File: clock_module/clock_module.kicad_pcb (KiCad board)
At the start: 2 copper layers, 100 x 100 mm, 38 parts, among them J1 USB_C_Receptacle_PowerOnly_6P, J2 Conn_01x02_Socket, SW1 SW_Push, SW2 SW_SPDT, SW3 SW_SPDT, SW4 SW_SPST, U1 74HC14

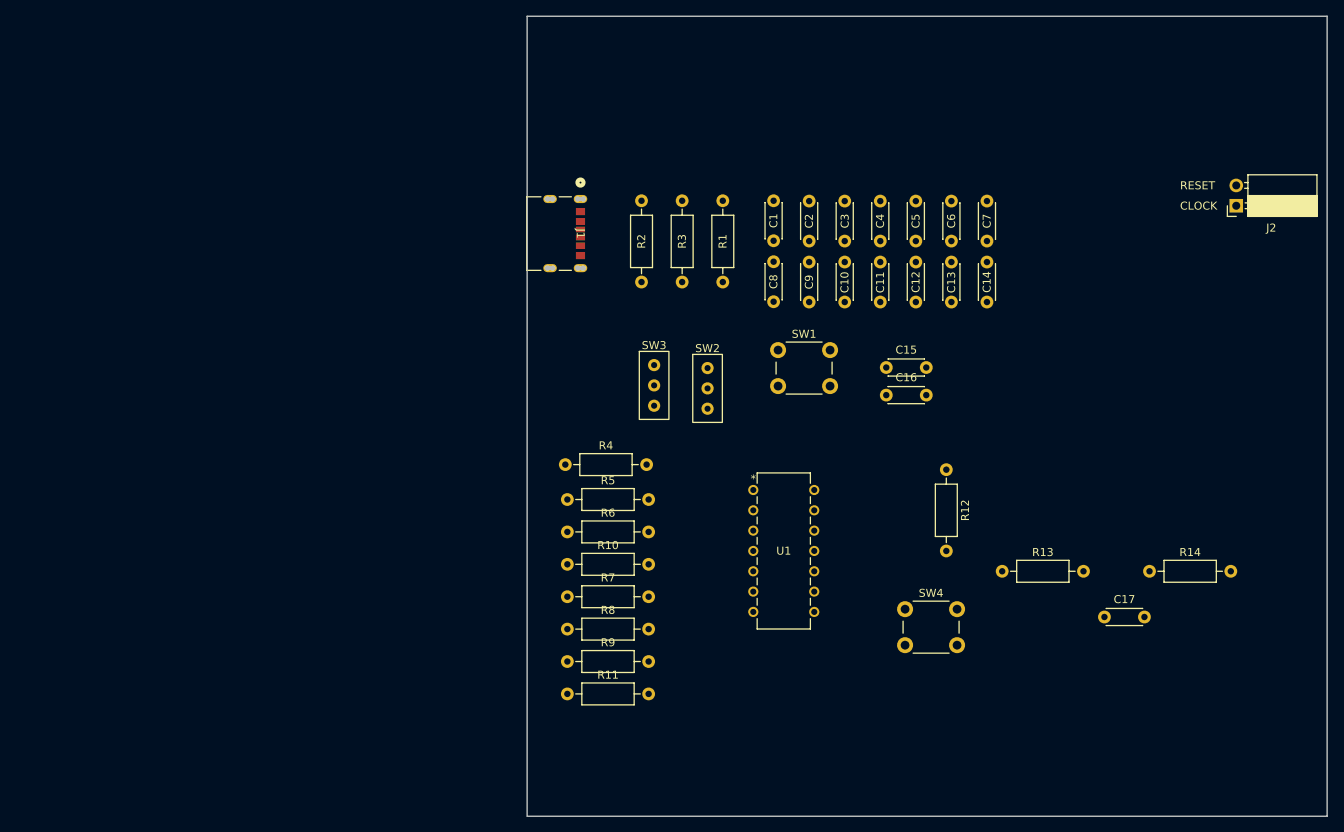
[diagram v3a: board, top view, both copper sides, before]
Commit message: クロック、リセット回路の基盤設計
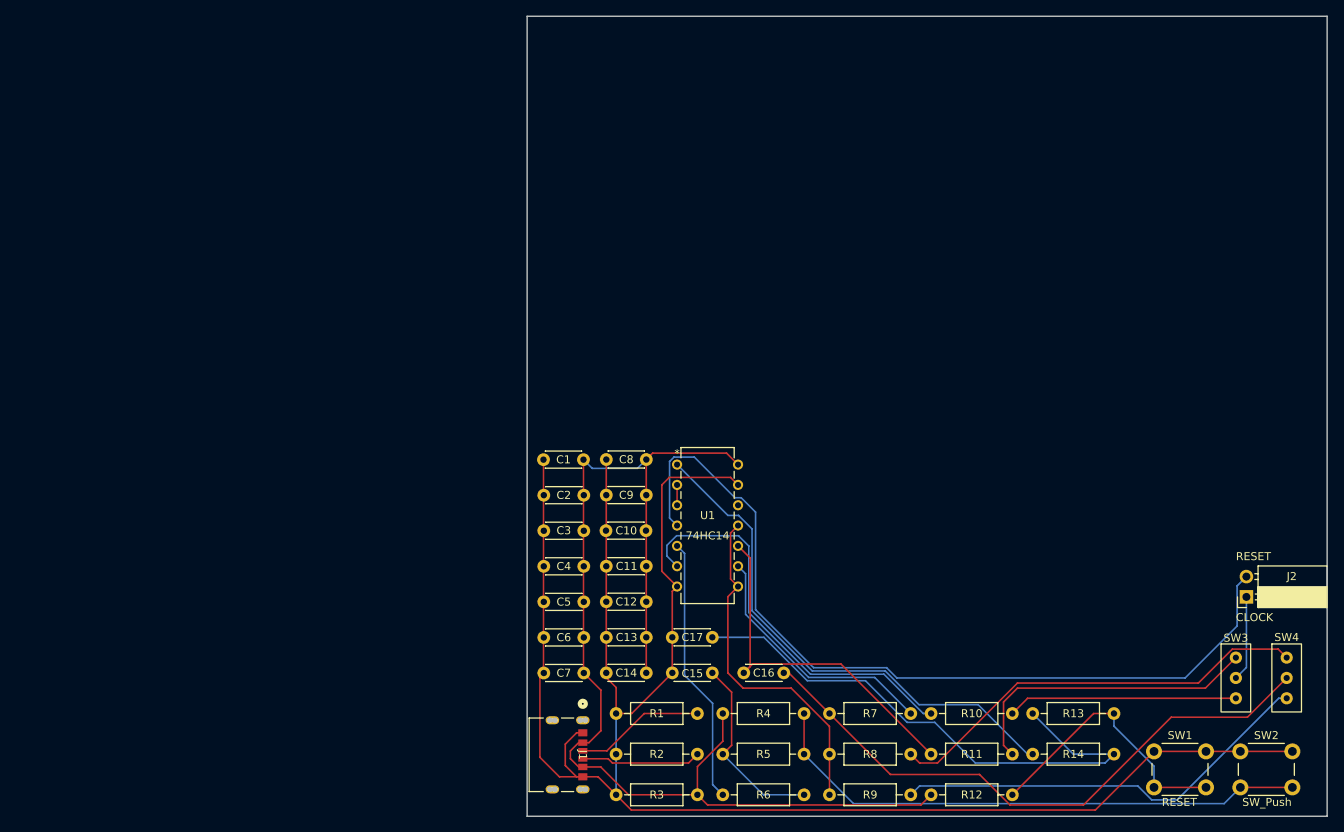
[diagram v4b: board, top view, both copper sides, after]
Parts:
- R1: value 1K -> 5.1K
- R3: value 5.1K -> 1K
- SW1: value SW_Push -> SW_SPST
- SW2: value SW_SPDT -> SW_Push; footprint footprint_library:SS-12D00G3 -> Button_Switch_THT:SW_PUSH_6mm
- SW4: value SW_SPST -> SW_SPDT; footprint Button_Switch_THT:SW_PUSH_6mm -> footprint_library:SS-12D00G3
- moved SW3 81.4 mm to (188.6, 132.7)
- moved SW2 80.6 mm to (189.2, 141.9)
- moved C7 73.9 mm to (107.1, 132.1), turned to 180 degrees
- moved SW1 68.7 mm to (178.4, 141.9)
- moved C6 67.6 mm to (107.1, 127.7), turned to 180 degrees
- moved J1 65.2 mm to (103.8, 142.3)
- moved R3 64.1 mm to (121.3, 147.3), turned to 180 degrees
- moved C14 62.9 mm to (114.9, 132.1), turned to 180 degrees
- moved C5 61.3 mm to (107.1, 123.2), turned to 180 degrees
- moved R2 59.4 mm to (121.3, 142.2), turned to 180 degrees
- moved C13 56.7 mm to (114.9, 127.6), turned to 180 degrees
- moved C4 55.0 mm to (107.1, 118.8), turned to 180 degrees
- moved R1 54.0 mm to (121.3, 137.2), turned to 180 degrees
- moved C12 50.4 mm to (114.9, 123.2), turned to 180 degrees
- moved R10 49.1 mm to (150.5, 137.2)
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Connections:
- C16 pad 1: Net-(SW2-B) -> Net-(SW4-B)
- R1 pad 1: +5V -> Net-(J1-CC1)
- R12 pad 2: Net-(SW4-B) -> Net-(SW1-B)
- R13 pad 1: Net-(SW4-B) -> Net-(SW1-B)
- R2 pad 1: Net-(J1-CC1) -> Net-(J1-CC2)
- R3 pad 1: Net-(J1-CC2) -> +5V
- R7 pad 1: Net-(SW2-B) -> Net-(SW4-B)
- R8 pad 1: Net-(SW2-A) -> Net-(SW4-A)
- R9 pad 1: Net-(SW2-C) -> Net-(SW4-C)
- SW1 pad 2: Net-(R4-Pad2) -> Net-(SW1-B)
- SW2 pad 1: Net-(SW2-A) -> GND
- SW2 pad 2: Net-(SW2-B) -> Net-(R4-Pad2)
- SW4 pad 1: GND -> Net-(SW4-A)
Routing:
- net GND: track 0.00 -> 231.1 mm
- net +5V: track 0.00 -> 147.9 mm
- net RESET: track 0.00 -> 107.5 mm
- net Net-(SW4-B): track 0.00 -> 76.3 mm
- net Net-(R4-Pad2): track 0.00 -> 69.5 mm
- net Net-(C17-Pad1): track 0.00 -> 69.4 mm
- net Net-(R14-Pad2): track 0.00 -> 65.4 mm
- net Net-(SW4-A): track 0.00 -> 53.8 mm
- net Net-(SW4-C): track 0.00 -> 53.4 mm
- net Net-(R10-Pad1): track 0.00 -> 50.7 mm
- net Net-(C16-Pad2): track 0.00 -> 45.4 mm
- net Net-(R8-Pad2): track 0.00 -> 43.7 mm
- net Net-(SW3-A): track 0.00 -> 38.3 mm
- net Net-(SW1-B): track 0.00 -> 34.7 mm
- net Net-(R6-Pad2): track 0.00 -> 33.5 mm
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
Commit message: 電源位置変更
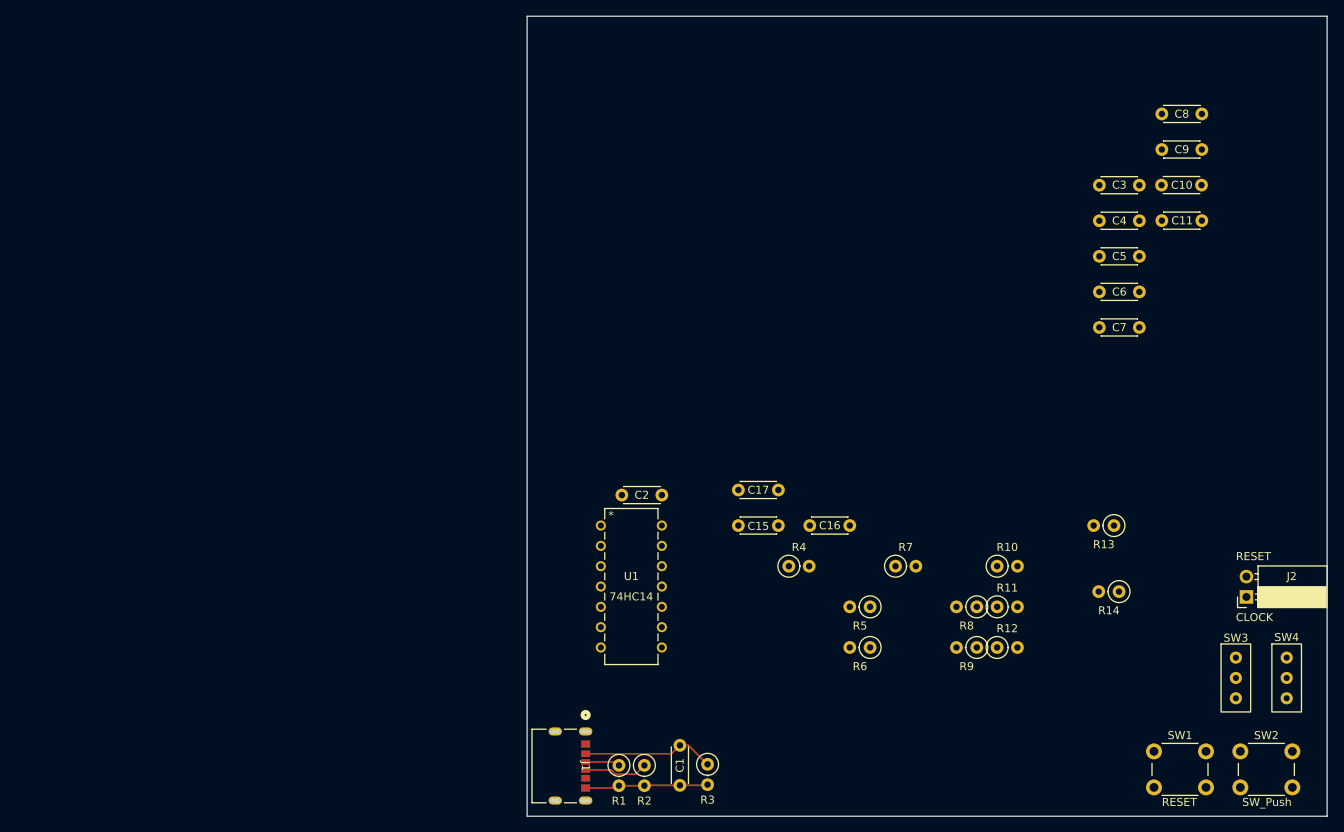
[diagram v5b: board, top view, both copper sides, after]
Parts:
- removed C12, C13, C14: 0.1uF, Capacitor_THT:C_Disc_D4.3mm_W1.9mm_P5.00mm
- R1, R10, R11, R12, R13, R14, R2, R3, R4, R5, R6, R7, R8, R9: footprint Resistor_THT:R_Axial_DIN0207_L6.3mm_D2.5mm_P10.16mm_Horizontal -> Resistor_THT:R_Axial_DIN0207_L6.3mm_D2.5mm_P2.54mm_Vertical
- moved C11 81.8 mm to (184.3, 75.5)
- moved C4 81.8 mm to (176.5, 75.6)
- moved C6 81.8 mm to (176.5, 84.5)
- moved C9 81.8 mm to (184.3, 66.7)
- moved C10 81.8 mm to (184.3, 71.1)
- moved C3 81.8 mm to (176.5, 71.1)
- moved C5 81.8 mm to (176.5, 80.0)
- moved C7 81.8 mm to (176.5, 88.9)
- moved C8 81.8 mm to (184.3, 62.2)
- moved C1 37.7 mm to (119.1, 141.1), turned to -90 degrees
- moved R13 23.5 mm to (173.4, 113.7)
- moved R14 20.3 mm to (174.0, 121.9)
- moved C15 20.2 mm to (131.4, 113.7)
- moved C16 20.2 mm to (140.3, 113.7)
- moved C17 20.2 mm to (131.4, 109.2)
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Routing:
- net GND: track 231.1 -> 15.4 mm
- net +5V: track 147.9 -> 16.7 mm
- net RESET: track 107.5 -> 0.00 mm
- net Net-(SW4-B): track 76.3 -> 0.00 mm
- net Net-(R4-Pad2): track 69.5 -> 0.00 mm
- net Net-(C17-Pad1): track 69.4 -> 0.00 mm
- net Net-(R14-Pad2): track 65.4 -> 0.00 mm
- net Net-(SW4-A): track 53.8 -> 0.00 mm
- net Net-(SW4-C): track 53.4 -> 0.00 mm
- net Net-(R10-Pad1): track 50.7 -> 0.00 mm
- net Net-(C16-Pad2): track 45.4 -> 0.00 mm
- net Net-(R8-Pad2): track 43.7 -> 0.00 mm
- net Net-(SW3-A): track 38.3 -> 0.00 mm
- net Net-(SW1-B): track 34.7 -> 0.00 mm
- net Net-(R6-Pad2): track 33.5 -> 0.00 mm
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
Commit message: 回路図からPCB更新
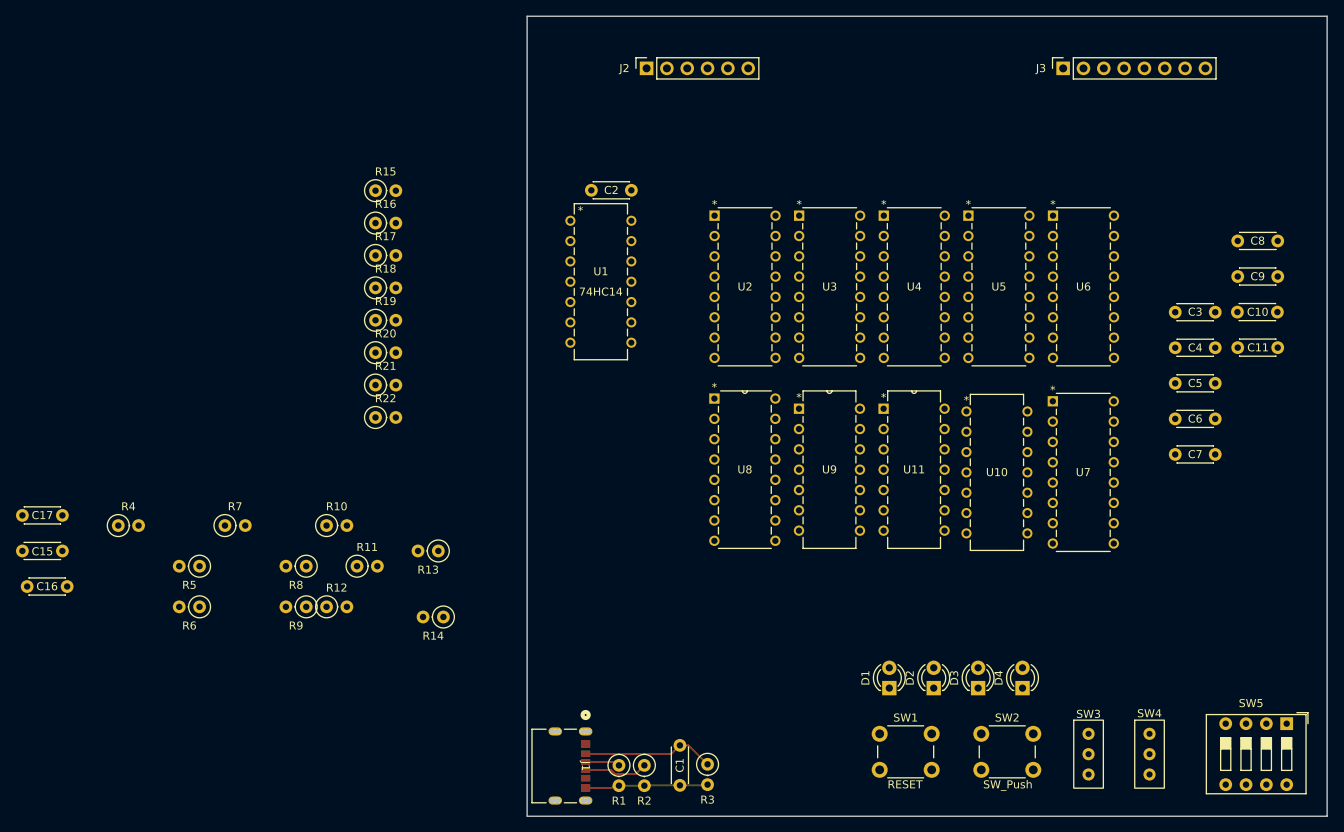
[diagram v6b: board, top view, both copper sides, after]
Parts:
- added D1: LED, LED_THT:LED_D3.0mm, F.Cu at (145.3, 134.0)
- added D2: LED, LED_THT:LED_D3.0mm, F.Cu at (150.8, 134.0)
- added D3: LED, LED_THT:LED_D3.0mm, F.Cu at (156.4, 134.0)
- added D4: LED, LED_THT:LED_D3.0mm, F.Cu at (161.9, 134.0)
- added J3: Conn_01x08_Socket, Connector_PinSocket_2.54mm:PinSocket_1x08_P2.54mm_Vertical, F.Cu at (167.0, 56.5)
- added R15: R, Resistor_THT:R_Axial_DIN0207_L6.3mm_D2.5mm_P2.54mm_Vertical, F.Cu at (81.0, 71.8)
- added R16: R, Resistor_THT:R_Axial_DIN0207_L6.3mm_D2.5mm_P2.54mm_Vertical, F.Cu at (81.0, 75.9)
- added R17: R, Resistor_THT:R_Axial_DIN0207_L6.3mm_D2.5mm_P2.54mm_Vertical, F.Cu at (81.0, 79.9)
- added R18: R, Resistor_THT:R_Axial_DIN0207_L6.3mm_D2.5mm_P2.54mm_Vertical, F.Cu at (81.0, 84.0)
- added R19: R, Resistor_THT:R_Axial_DIN0207_L6.3mm_D2.5mm_P2.54mm_Vertical, F.Cu at (81.0, 88.0)
- added R20: R, Resistor_THT:R_Axial_DIN0207_L6.3mm_D2.5mm_P2.54mm_Vertical, F.Cu at (81.0, 92.1)
- added R21: R, Resistor_THT:R_Axial_DIN0207_L6.3mm_D2.5mm_P2.54mm_Vertical, F.Cu at (81.0, 96.1)
- added R22: R, Resistor_THT:R_Axial_DIN0207_L6.3mm_D2.5mm_P2.54mm_Vertical, F.Cu at (81.0, 100.2)
- added SW5: SW_DIP_x04, Button_Switch_THT:SW_DIP_SPSTx04_Slide_9.78x12.34mm_W7.62mm_P2.54mm, F.Cu at (194.9, 138.4)
- added U10: 74HC74, footprint_library:DIP14_TOS, F.Cu at (154.9, 99.4)
- added U11: 74HC10, footprint_library:74hc10, F.Cu at (152.2, 114.3)
- added U2: 74HC161N, footprint_library:74hc161, F.Cu at (123.4, 74.9)
- added U3: 74HC161N, footprint_library:74hc161, F.Cu at (134.0, 74.9)
- added U4: 74HC161N, footprint_library:74hc161, F.Cu at (144.6, 74.9)
- added U5: 74HC161N, footprint_library:74hc161, F.Cu at (155.2, 74.9)
- added U6: 74HC153, footprint_library:SOT38-4_NEX, F.Cu at (165.7, 74.9)
- added U7: 74HC153, footprint_library:SOT38-4_NEX, F.Cu at (165.7, 98.1)
- added U8: 74HC283, footprint_library:74hc283, F.Cu at (131.0, 115.6)
- added U9: 74HC32, footprint_library:74hc32, F.Cu at (141.6, 114.3)
- J2: value Conn_01x02_Socket -> Conn_01x06_Socket; footprint Connector_PinSocket_2.54mm:PinSocket_1x02_P2.54mm_Horizontal -> Connector_PinSocket_2.54mm:PinSocket_1x06_P2.54mm_Vertical
- moved J2 99.9 mm to (114.9, 56.5), turned to 90 degrees
- moved C16 98.1 mm to (42.5, 121.3)
- moved C15 89.6 mm to (41.9, 116.8)
- moved C17 89.6 mm to (41.9, 112.4)
- moved R14 84.5 mm to (89.5, 125.1)
- moved R13 84.5 mm to (88.9, 116.8)
- moved R7 84.0 mm to (62.2, 113.7)
- moved R8 84.0 mm to (72.4, 118.7)
- moved R9 84.0 mm to (72.4, 123.8)
- moved R10 84.0 mm to (74.9, 113.7)
- moved R12 84.0 mm to (74.9, 123.8)
- moved R4 84.0 mm to (48.9, 113.7)
- moved R5 84.0 mm to (59.1, 118.7)
- moved R6 84.0 mm to (59.1, 123.8)
- moved R11 80.2 mm to (78.7, 118.7)
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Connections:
- J2 pad 1: CLOCK -> A0
- J2 pad 2: RESET -> A1
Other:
- board text removed: "CLOCK"
- board text removed: "RESET"

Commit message: コネクタを平面に変更
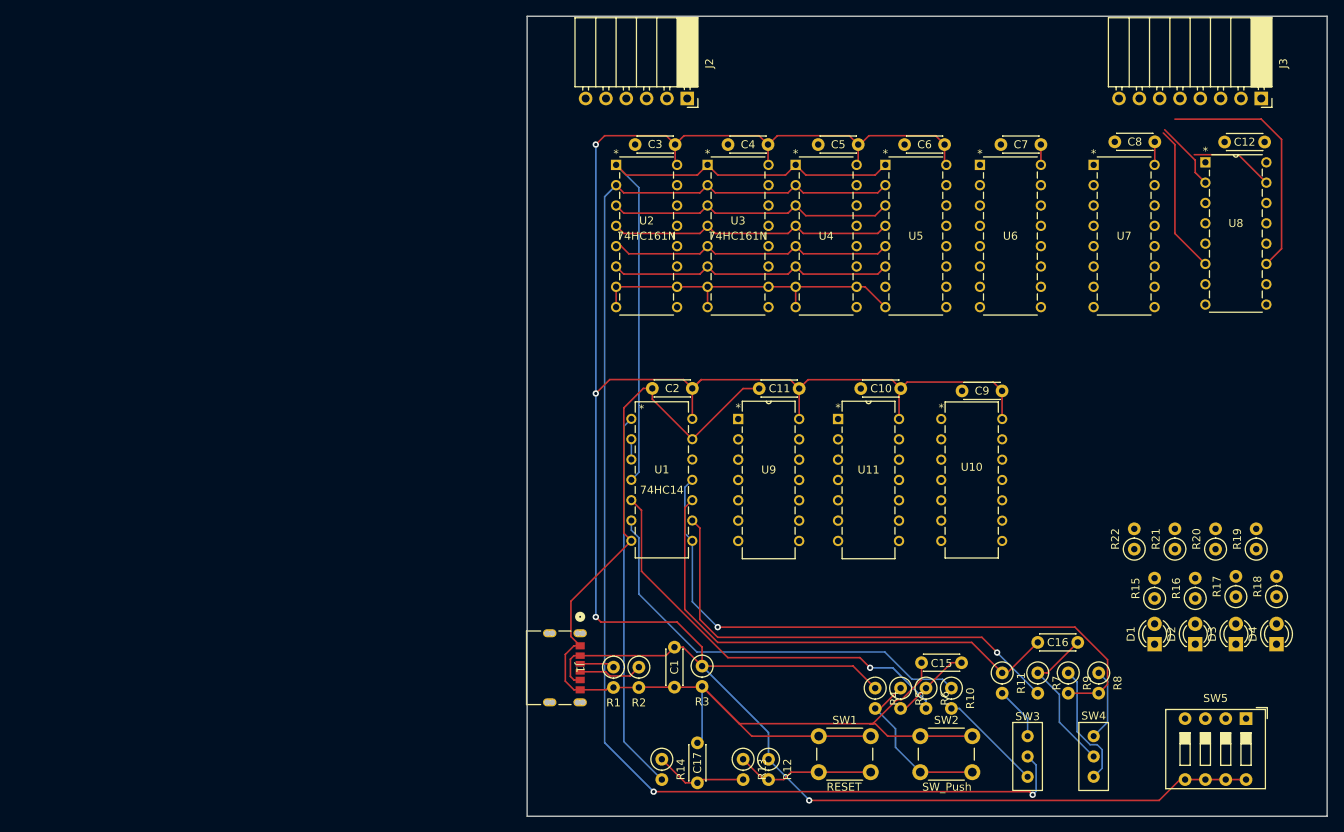
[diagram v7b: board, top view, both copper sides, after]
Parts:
- added C12: 0.1uF, Capacitor_THT:C_Disc_D4.3mm_W1.9mm_P5.00mm, F.Cu at (192.2, 65.7)
- J2: footprint Connector_PinSocket_2.54mm:PinSocket_1x06_P2.54mm_Vertical -> Connector_PinSocket_2.54mm:PinSocket_1x06_P2.54mm_Horizontal
- J3: footprint Connector_PinSocket_2.54mm:PinSocket_1x08_P2.54mm_Vertical -> Connector_PinSocket_2.54mm:PinSocket_1x08_P2.54mm_Horizontal
- moved C16 126.5 mm to (168.8, 128.3)
- moved R18 119.1 mm to (193.7, 122.6), turned to 90 degrees
- moved R17 115.7 mm to (188.6, 122.6), turned to 90 degrees
- moved R19 113.7 mm to (191.1, 116.6), turned to 90 degrees
- moved C15 113.3 mm to (154.3, 130.8)
- moved R16 112.7 mm to (183.5, 122.8), turned to 90 degrees
- moved R15 109.9 mm to (178.4, 122.8), turned to 90 degrees
- moved R20 107.8 mm to (186.1, 116.6), turned to 90 degrees
- moved R7 103.3 mm to (163.8, 132.1), turned to -90 degrees
- moved R21 102.0 mm to (181.0, 116.6), turned to 90 degrees
- moved R8 100.0 mm to (171.4, 132.1), turned to -90 degrees
- moved R4 96.8 mm to (143.5, 134.0), turned to -90 degrees
- moved R22 96.3 mm to (175.9, 116.6), turned to 90 degrees
- moved R9 95.6 mm to (167.6, 132.1), turned to -90 degrees
- moved R6 91.4 mm to (149.9, 134.0), turned to -90 degrees
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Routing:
- net +5V: track 16.7 -> 333.0 mm, vias 0 -> 4
- net GND: track 15.4 -> 201.5 mm
- net CLOCK: track 0.00 -> 167.9 mm, vias 0 -> 2
- net Net-(R8-Pad2): track 0.00 -> 79.4 mm, vias 0 -> 1
- net RESET: track 0.00 -> 77.7 mm
- net Net-(C16-Pad2): track 0.00 -> 63.0 mm
- net Net-(R7-Pad2): track 0.00 -> 58.8 mm, vias 0 -> 1
- net Net-(R10-Pad1): track 0.00 -> 53.5 mm
- net Net-(R6-Pad2): track 0.00 -> 52.6 mm, vias 0 -> 1
- net Net-(R14-Pad2): track 0.00 -> 47.4 mm
- net Net-(U2-D0): track 0.00 -> 36.3 mm
- net Net-(U2-D3): track 0.00 -> 36.2 mm
- net Net-(U2-D2): track 0.00 -> 36.0 mm
- net Net-(U2-D1): track 0.00 -> 36.0 mm
- net D3: track 0.00 -> 30.7 mm
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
